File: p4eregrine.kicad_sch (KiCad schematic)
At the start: 45 parts, among them U1 ESP32-P4NRW32X, U15 TPD2EUSB30A, U3 W25Q128JVP, Y1 Crystal_GND24

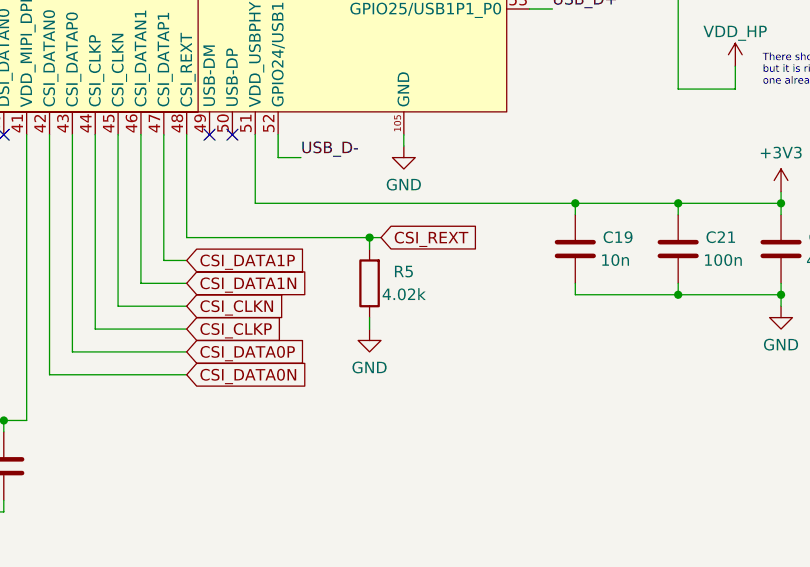
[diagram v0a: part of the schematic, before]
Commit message: Reduce BOM by a couple of resistors
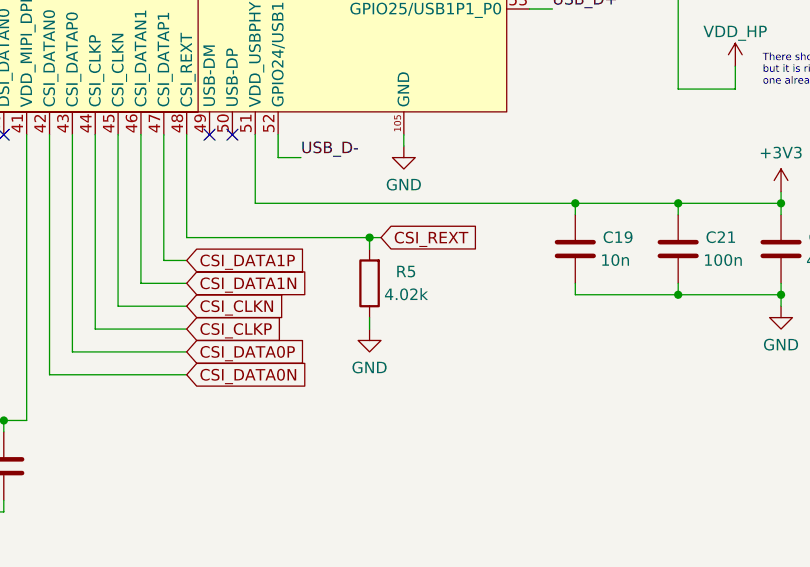
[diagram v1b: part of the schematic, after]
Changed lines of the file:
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@@
 		(dnp no)
 		(property "Reference" "R5"
-			(at 176.53 228.6 0)
+			(at 176.784 228.6 0)
 			(show_name no)
 			(do_not_autoplace no)
@@
 		)
 		(property "Value" "4.02k"
-			(at 176.53 231.14 0)
+			(at 176.784 231.14 0)
 			(show_name no)
 			(do_not_autoplace no)

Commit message: Get rid of 4.7uf caps and add missing MPNs to BOM
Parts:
- C1: MPN (none) -> GRM21BZ71E106KE15L
- C10, C14, C15, C16, C17, C2, C20, C21, C22, C23, C26, C3, C34, C4, C62: MPN (none) -> GRM033R61E104KE14D
- C11, C12: MPN (none) -> CC0402FRNPO9BN120
- C13, C19: LCSC Part C15195 -> C85930; MPN (none) -> GRM033R71E103KE14D
- C18, C29, C32, C33, C7: MPN (none) -> CL05A105KA5NQNC
- C25: value 4.7u -> 10u
- C27, C8: MPN (none) -> CL10B106MQ8NRNC
- D1: MPN (none) -> XL-0201UYC
- R1, R12, R6, R7: MPN (none) -> 0201WMF1002TEE
- R10, R11, R2, R49, R51: MPN (none) -> 0201WMF4701TEE
- R5: MPN (none) -> NQ01WMF4021TEE
- U1: MPN (none) -> ESP32-P4NRW32X
- U15: MPN (none) -> TPD2EUSB30ADRTR
- U3: MPN (none) -> W25Q128JVPIM
- Y1: MPN (none) -> XTM20040000FT00351001

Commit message: Fix some typos in comments and BOM description
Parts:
- C25: LCSC Part C19666 -> C3039698; MPN (none) -> CL10B106MQ8NRNC
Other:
- note added: "Using 4.7k CC resistors to minimize BOM which is still within USB-C specs"
- note removed: "Using 4.7kCC resistors to minimize BOM which is still within USB-C specs"
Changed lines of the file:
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@@
 		)
 	)
-	(text "Using 4.7kCC  resistors to minimize BOM\nwhich is still within USB-C specs"
+	(text "Using 4.7k CC  resistors to minimize BOM\nwhich is still within USB-C specs"
 		(exclude_from_sim no)
 		(at 274.066 83.058 0)
@@
 			)
 		)
-		(property "LCSC Part" "C19666"
+		(property "LCSC Part" "C3039698"
 			(at 218.44 226.06 0)
 			(hide yes)
@@
 			(at 218.44 226.06 0)
 			(hide yes)
+			(show_name no)
+			(do_not_autoplace no)
+			(effects
+				(font
+					(size 1.27 1.27)
+				)
+			)
+		)
+		(property "MPN" "CL10B106MQ8NRNC"
+			(at 218.44 226.06 0)
+			(hide yes)

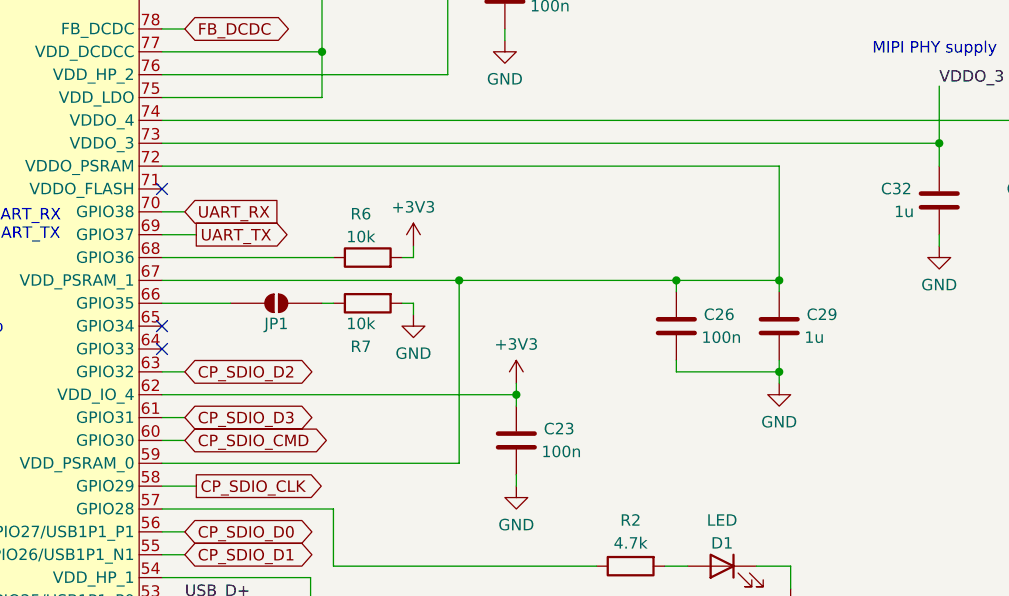
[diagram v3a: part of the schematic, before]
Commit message: Change crystals to more available parts
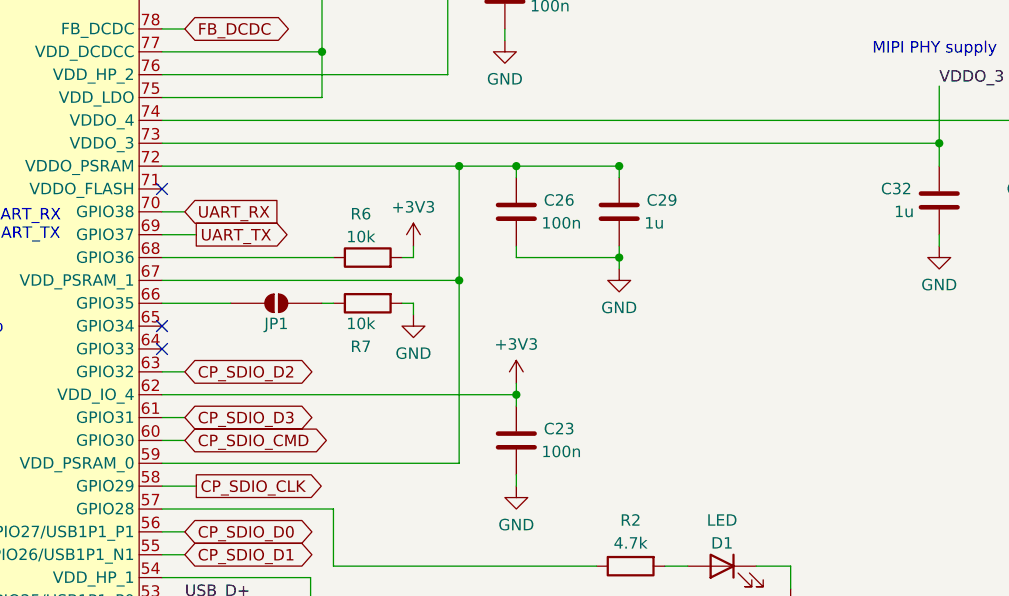
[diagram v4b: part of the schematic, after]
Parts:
- Y1: LCSC Part C37635335 -> C20612989; MPN XTM20040000FT00351001 -> SX20Y040000B91T008
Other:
- moved on the sheet: C26, C29
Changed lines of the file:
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@@
 	)
 	(junction
-		(at 223.52 163.83)
-		(diameter 0)
-		(color 0 0 0 0)
-	)
-	(junction
 		(at 105.41 114.3)
 		(diameter 0)
@@
 	)
 	(junction
+		(at 223.52 151.13)
+		(diameter 0)
+		(color 0 0 0 0)
+	)
+	(junction
 		(at 93.98 93.98)
 		(diameter 0)
@@
 	)
 	(junction
+		(at 223.52 163.83)
+		(diameter 0)
+		(color 0 0 0 0)
+	)
+	(junction
 		(at 109.22 255.27)
 		(diameter 0)
@@
 	)
 	(junction
-		(at 247.65 163.83)
+		(at 229.87 151.13)
 		(diameter 0)
 		(color 0 0 0 0)
@@
 	)
 	(junction
-		(at 259.08 163.83)
+		(at 241.3 151.13)
 		(diameter 0)
 		(color 0 0 0 0)
@@
 	)
 	(junction
-		(at 259.08 173.99)
+		(at 241.3 161.29)
 		(diameter 0)
 		(color 0 0 0 0)
@@
 	(wire
 		(pts
-			(xy 259.08 163.83) (xy 259.08 165.1)
+			(xy 241.3 151.13) (xy 241.3 152.4)
 		)
 		(stroke
@@
 	(wire
 		(pts
-			(xy 259.08 173.99) (xy 259.08 175.26)
+			(xy 241.3 161.29) (xy 241.3 162.56)
 		)
 		(stroke
@@
 	(wire
 		(pts
-			(xy 247.65 173.99) (xy 259.08 173.99)
+			(xy 229.87 161.29) (xy 241.3 161.29)
 		)
 		(stroke
@@
 	(wire
 		(pts
-			(xy 259.08 151.13) (xy 259.08 163.83)
-		)
-		(stroke
-			(width 0)
-			(type default)
-		)
-	)
-	(wire
-		(pts
 			(xy 109.22 254) (xy 109.22 255.27)
 		)
@@
 	(wire
 		(pts
+			(xy 223.52 151.13) (xy 223.52 163.83)
+		)
+		(stroke
+			(width 0)
+			(type default)
+		)
+	)
+	(wire
+		(pts
 			(xy 114.3 124.46) (xy 114.3 73.66)
 		)
@@
 	(wire
 		(pts
-			(xy 247.65 163.83) (xy 247.65 165.1)
+			(xy 229.87 151.13) (xy 229.87 152.4)
 		)
 		(stroke
@@
 	(wire
 		(pts
-			(xy 223.52 163.83) (xy 247.65 163.83)
+			(xy 223.52 151.13) (xy 241.3 151.13)
 		)
 		(stroke
@@
 	(wire
 		(pts
-			(xy 247.65 172.72) (xy 247.65 173.99)
+			(xy 229.87 160.02) (xy 229.87 161.29)
 		)
 		(stroke
@@
 	(wire
 		(pts
-			(xy 259.08 172.72) (xy 259.08 173.99)
+			(xy 241.3 160.02) (xy 241.3 161.29)
 		)
 		(stroke
@@
 	(wire
 		(pts
-			(xy 190.5 151.13) (xy 259.08 151.13)
+			(xy 190.5 151.13) (xy 223.52 151.13)
 		)
 		(stroke
@@
 	(wire
 		(pts
-			(xy 247.65 163.83) (xy 259.08 163.83)
-		)
-		(stroke
-			(width 0)
-			(type default)
-		)
-	)
-	(wire
-		(pts
 			(xy 104.14 58.42) (xy 104.14 59.69)
 		)
@@
 	(symbol
 		(lib_id "Device:C")
-		(at 259.08 168.91 0)
+		(at 241.3 156.21 0)
 		(unit 1)
 		(body_style 1)
@@
 		(dnp no)
 		(property "Reference" "C29"
-			(at 262.128 167.64 0)
+			(at 244.348 154.94 0)
 			(show_name no)
 			(do_not_autoplace no)
@@
 		)
 		(property "Value" "1u"
-			(at 261.874 170.18 0)
+			(at 244.094 157.48 0)
 			(show_name no)
 			(do_not_autoplace no)
@@
 		)
 		(property "Footprint" "Capacitor_SMD:C_0402_1005Metric"
-			(at 260.0452 172.72 0)
+			(at 242.2652 160.02 0)
 			(hide yes)
 			(show_name no)
@@
 		)
 		(property "Datasheet" ""
-			(at 259.08 168.91 0)
+			(at 241.3 156.21 0)
 			(hide yes)
 			(show_name no)
@@
 		)
 		(property "Description" "Unpolarized capacitor"
-			(at 259.08 168.91 0)
+			(at 241.3 156.21 0)
 			(hide yes)
 			(show_name no)
@@
 		)
 		(property "KLC_S3.3" ""
-			(at 259.08 168.91 0)
+			(at 241.3 156.21 0)
 			(hide yes)
 			(show_name no)
@@
 		)
 		(property "KLC_S4.1" ""
-			(at 259.08 168.91 0)
+			(at 241.3 156.21 0)
 			(hide yes)
 			(show_name no)
@@
 		)
 		(property "KLC_S5.1" ""
-			(at 259.08 168.91 0)
+			(at 241.3 156.21 0)
 			(hide yes)
 			(show_name no)
@@
 		)
 		(property "LCSC Part" "C52923"
-			(at 259.08 168.91 0)
+			(at 241.3 156.21 0)
 			(hide yes)
 			(show_name no)
@@
 		)
 		(property "MPN" "CL05A105KA5NQNC"
-			(at 259.08 168.91 0)
+			(at 241.3 156.21 0)
 			(hide yes)
 			(show_name no)
@@
 	(symbol
 		(lib_id "Device:C")
-		(at 247.65 168.91 0)
+		(at 229.87 156.21 0)
 		(unit 1)
 		(body_style 1)
@@
 		(dnp no)
 		(property "Reference" "C26"
-			(at 250.698 167.64 0)
+			(at 232.918 154.94 0)
 			(show_name no)
 			(do_not_autoplace no)
@@
 		)
 		(property "Value" "100n"
-			(at 250.444 170.18 0)
+			(at 232.664 157.48 0)
 			(show_name no)
 			(do_not_autoplace no)
@@
 		)
 		(property "Footprint" "Capacitor_SMD:C_0201_0603Metric"
-			(at 248.6152 172.72 0)
+			(at 230.8352 160.02 0)
 			(hide yes)
 			(show_name no)
@@
 		)
 		(property "Datasheet" ""
-			(at 247.65 168.91 0)
+			(at 229.87 156.21 0)
 			(hide yes)
 			(show_name no)
@@
 		)
 		(property "Description" "Unpolarized capacitor"
-			(at 247.65 168.91 0)
+			(at 229.87 156.21 0)
 			(hide yes)
 			(show_name no)
@@
 		)
 		(property "KLC_S3.3" ""
-			(at 247.65 168.91 0)
+			(at 229.87 156.21 0)
 			(hide yes)
 			(show_name no)
@@
 		)
 		(property "KLC_S4.1" ""
-			(at 247.65 168.91 0)
+			(at 229.87 156.21 0)
 			(hide yes)
 			(show_name no)
@@
 		)
 		(property "KLC_S5.1" ""
-			(at 247.65 168.91 0)
+			(at 229.87 156.21 0)
 			(hide yes)
 			(show_name no)
@@
 		)
 		(property "LCSC Part" "C76939"
-			(at 247.65 168.91 0)
+			(at 229.87 156.21 0)
 			(hide yes)
 			(show_name no)
@@
 		)
 		(property "MPN" "GRM033R61E104KE14D"
-			(at 247.65 168.91 0)
+			(at 229.87 156.21 0)
 			(hide yes)
 			(show_name no)
@@
 	(symbol
 		(lib_id "power:GND")
-		(at 259.08 175.26 0)
+		(at 241.3 162.56 0)
 		(mirror y)
 		(unit 1)
@@
 		(dnp no)
 		(property "Reference" "#PWR037"
-			(at 259.08 181.61 0)
+			(at 241.3 168.91 0)
 			(hide yes)
 			(show_name no)
@@
 		)
 		(property "Value" "GND"
-			(at 259.08 179.578 0)
+			(at 241.3 166.878 0)
 			(show_name no)
 			(do_not_autoplace no)
@@
 		)
 		(property "Footprint" ""
-			(at 259.08 175.26 0)
+			(at 241.3 162.56 0)
 			(hide yes)
 			(show_name no)
@@
 		)
 		(property "Datasheet" ""
-			(at 259.08 175.26 0)
+			(at 241.3 162.56 0)
 			(hide yes)
 			(show_name no)
@@
 		)
 		(property "Description" "Power symbol creates a global label with name \"GND\" , ground"
-			(at 259.08 175.26 0)
+			(at 241.3 162.56 0)
 			(hide yes)
 			(show_name no)
@@
 			)
 		)
-		(property "LCSC Part" "C37635335"
+		(property "LCSC Part" "C20612989"
 			(at 110.49 49.53 0)
 			(hide yes)
@@
 			)
 		)
-		(property "MPN" "XTM20040000FT00351001"
+		(property "MPN" "SX20Y040000B91T008"
 			(at 110.49 49.53 0)
 			(hide yes)
